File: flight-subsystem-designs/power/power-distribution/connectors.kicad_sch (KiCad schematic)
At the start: 36 parts, among them J1 Conn_02x07_Top_Bottom, J10 Conn_01x04, J2 Conn_02x26_Odd_Even, J3 Conn_01x02, J4 Conn_01x02, J5 Conn_01x02, J6 Conn_01x02, J7 Conn_02x26_Odd_Even, J8 Conn_01x04, J9 Conn_01x04, Q1 NMOS, Q2 NMOS

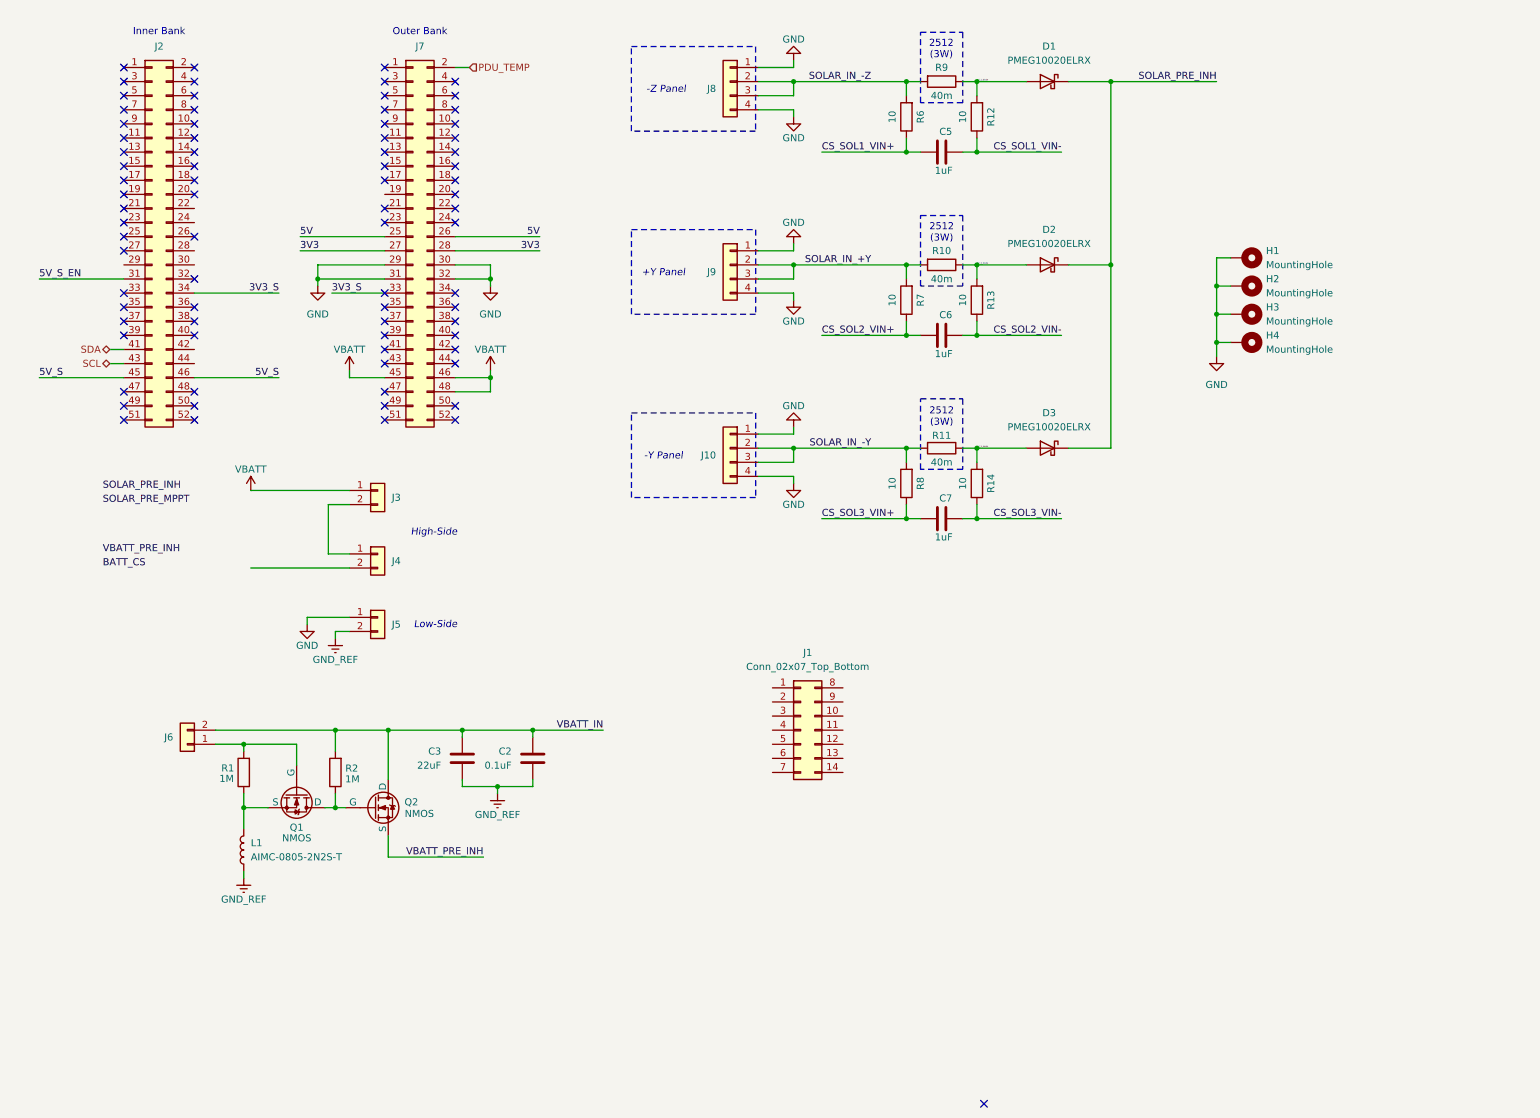
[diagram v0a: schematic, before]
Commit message: feat: PDU 4.0.0 (WIP)
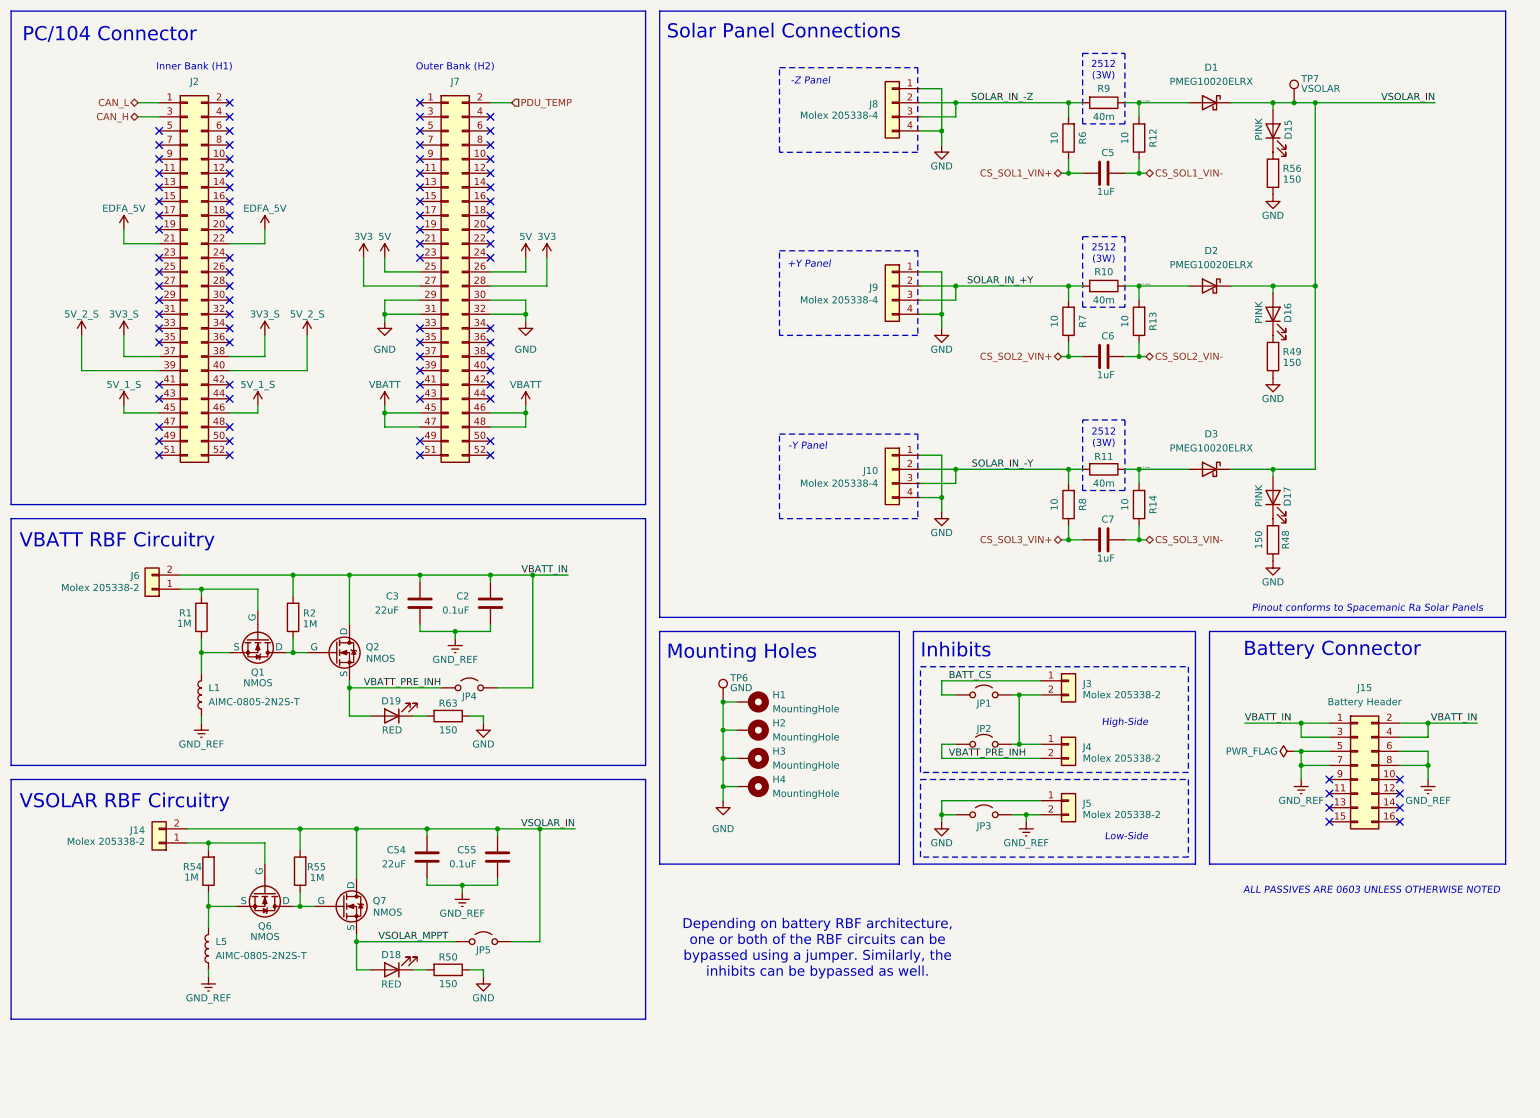
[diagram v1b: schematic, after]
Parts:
- removed J1: Conn_02x07_Top_Bottom, Connector_Harwin:Harwin_LTek-Male_2x07_P2.00mm_Vertical_StrainRelief, symbol Connector_Generic:Conn_02x07_Top_Bottom
- added C54: 22uF, Capacitor_SMD:C_0805_2012Metric, symbol Device:C
- added C55: 0.1uF, Capacitor_SMD:C_0805_2012Metric, symbol Device:C
- added D15, D16, D17: PINK, LED_SMD:LED_0603_1608Metric, symbol Device:LED
- added D18, D19: RED, LED_SMD:LED_0603_1608Metric, symbol Device:LED
- added J14: Molex 205338-2, Connector_Molex:Molex_Pico-Lock_205338-0002_1x02-1MP_P2.00mm_Horizontal, symbol Connector_Generic:Conn_01x02
- added J15: Battery Header, Connector_PinHeader_2.54mm:PinHeader_2x08_P2.54mm_Vertical, symbol Connector_Generic:Conn_02x08_Odd_Even
- added JP1, JP2, JP3, JP4, JP5: Jumper_2_Open, Jumper:SolderJumper-2_P1.3mm_Open_TrianglePad1.0x1.5mm, symbol Jumper:Jumper_2_Open
- added L5: AIMC-0805-2N2S-T, Inductor_SMD:L_0805_2012Metric, symbol Device:L
- added Q6, Q7: NMOS, Package_TO_SOT_SMD:TSOT-23, symbol Simulation_SPICE:NMOS
- added R48, R49, R50, R56, R63: 150, Resistor_SMD:R_0603_1608Metric, symbol Device:R
- added R54, R55: 1M, Resistor_SMD:R_0603_1608Metric, symbol Device:R
- added TP6: GND, TestPoint:TestPoint_Keystone_5000-5004_Miniature, symbol Connector:TestPoint
- added TP7: VSOLAR, TestPoint:TestPoint_Keystone_5000-5004_Miniature, symbol Connector:TestPoint
- J10, J8, J9: value Conn_01x04 -> Molex 205338-4
- J3, J4, J5: value Conn_01x02 -> Molex 205338-2
- J6: value Conn_01x02 -> Molex 205338-2; footprint (none) -> Connector_Molex:Molex_Pico-Lock_205338-0002_1x02-1MP_P2.00mm_Horizontal
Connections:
- net 3V3_S: now also J2.37 (Pin_37), J2.38 (Pin_38); no longer J2.34 (Pin_34), J7.33 (Pin_33)
- net BATT_CS: now also J3.1 (Pin_1), JP1.1 (A)
- net GND: now also JP3.1 (A), R48.1, R49.1, R50.1, R56.1, R63.1, TP6.1
- net GND_REF: now also C54.1, C55.1, J15.5 (Pin_5), J15.6 (Pin_6), J15.7 (Pin_7), J15.8 (Pin_8), JP3.2 (B), L5.1
- net VBATT: now also J7.47 (Pin_47); no longer J3.1 (Pin_1)
- net VBATT_IN: now also J15.1 (Pin_1), J15.2 (Pin_2), J15.3 (Pin_3), J15.4 (Pin_4), JP4.2 (B)
- net VBATT_PRE_INH: now also J4.2 (Pin_2), D19.2 (A), JP2.1 (A), JP4.1 (A)
- net at J3.2 (Pin_2), J4.1 (Pin_1): now also JP1.2 (B), JP2.2 (B)
- net CAN_L: now reaches J2.1 (Pin_1)
- net EDFA_5V: now reaches J2.21 (Pin_21)
- net EDFA_5V: now also J2.22 (Pin_22)
- net CAN_H: now reaches J2.3 (Pin_3)
- net 5V_2_S: now reaches J2.39 (Pin_39)
- net 5V_2_S: now also J2.40 (Pin_40)
- net 5V_S renamed 5V_1_S
- net 5V_S_EN: no longer names the net of J2.31 (Pin_31)
- net SCL: no longer names the net of J2.43 (Pin_43)
- net SDA: no longer names the net of J2.41 (Pin_41)
- net SOLAR_PRE_INH renamed VSOLAR_IN
- net VSOLAR_IN: now also C54.2, C55.2, D15.2 (A), D16.2 (A), D17.2 (A), J14.2 (Pin_2), JP5.2 (B), Q7.1 (D), R55.2, TP7.1
- new net: Q6.1 (D), Q7.2 (G), R55.1
- new net: D18.1 (K), R50.2
- new net: D16.1 (K), R49.2
- new net: J14.1 (Pin_1), Q6.2 (G), R54.2
- new net: D19.1 (K), R63.2
- new net: D17.1 (K), R48.2
- new net: L5.2, Q6.3 (S), R54.1
- new net: D15.1 (K), R56.2
- new net VSOLAR_MPPT: D18.2 (A), JP5.1 (A), Q7.3 (S)
- no-connect marks 79 -> 89
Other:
- note added: "ALL PASSIVES ARE 0603 UNLESS OTHERWISE NOTED"
- note added: "Battery Connector"
- note added: "Depending on battery RBF architecture, one or both of the RBF circuits can be bypassed using a jumper. Similarly, the inhibits can be bypassed as well."
- note added: "Inhibits"
- note added: "Inner Bank (H1)"
- note added: "Mounting Holes"
- note added: "Outer Bank (H2)"
- note added: "PC/104 Connector"
- note added: "Pinout conforms to Spacemanic Ra Solar Panels"
- note added: "Solar Panel Connections"
- note added: "VBATT RBF Circuitry"
- note added: "VSOLAR RBF Circuitry"
- note removed: "Inner Bank"
- note removed: "Outer Bank"
- moved on the sheet: C2, C3, C5, C6, C7, D1, D2, D3, H1, H2, H3, H4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

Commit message: shi
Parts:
- removed C2, C55: 0.1uF, Capacitor_SMD:C_0805_2012Metric, symbol Device:C
- removed C3, C54: 22uF, Capacitor_SMD:C_0805_2012Metric, symbol Device:C
- removed D18, D19: RED, LED_SMD:LED_0603_1608Metric, symbol Device:LED
- removed J14, J3, J4, J5, J6: Molex 205338-2, Connector_Molex:Molex_Pico-Lock_205338-0002_1x02-1MP_P2.00mm_Horizontal, symbol Connector_Generic:Conn_01x02
- removed JP1, JP2, JP3, JP4, JP5: Jumper_2_Open, Jumper:SolderJumper-2_P1.3mm_Open_TrianglePad1.0x1.5mm, symbol Jumper:Jumper_2_Open
- removed L1, L5: AIMC-0805-2N2S-T, Inductor_SMD:L_0805_2012Metric, symbol Device:L
- removed Q1, Q2, Q6, Q7: NMOS, Package_TO_SOT_SMD:TSOT-23, symbol Simulation_SPICE:NMOS
- removed R1, R2, R54, R55: 1M, Resistor_SMD:R_0603_1608Metric, symbol Device:R
- removed R50, R63: 150, Resistor_SMD:R_0603_1608Metric, symbol Device:R
- added J13, J19: RBF, Connector_Molex:Molex_PicoBlade_53047-0210_1x02_P1.25mm_Vertical, symbol Connector_Generic:Conn_01x02
- added J16, J17: NO, Connector_Molex:Molex_PicoBlade_53047-0210_1x02_P1.25mm_Vertical, symbol Connector_Generic:Conn_01x02
- added J18: NC, Connector_Molex:Molex_PicoBlade_53047-0210_1x02_P1.25mm_Vertical, symbol Connector_Generic:Conn_01x02
- added Q8: PMOS, Package_SO:TSOP-6_1.65x3.05mm_P0.95mm, symbol Simulation_SPICE:PMOS
- added Q9: NMOS, Package_SO:TSOP-6_1.65x3.05mm_P0.95mm, symbol Simulation_SPICE:NMOS
- added R64, R65, R66: 100k, Resistor_SMD:R_0603_1608Metric, symbol Device:R
- added U22: SI3407DV, Package_SO:TSOP-6_1.65x3.05mm_P0.95mm, symbol pdu:SI3407DV-T1-GE3
- J10, J8, J9: footprint Connector_Molex:Molex_Pico-Lock_205338-0004_1x04-1MP_P2.00mm_Horizontal -> Connector_Molex:Molex_PicoBlade_53047-0410_1x04_P1.25mm_Vertical
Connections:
- net BATT_CS: now also Q8.1 (D), Q8.2 (D), Q8.5 (D), Q8.6 (D)
- net GND: now also J13.1 (Pin_1), J16.1 (Pin_1), J17.1 (Pin_1), J19.1 (Pin_1), Q9.3 (S), R65.1
- net GND_REF: now also Q9.1 (D)
- net VBATT: now also J18.2 (Pin_2)
- net VBATT_IN: now also Q8.4 (S), R64.1
- net VSOLAR_IN: now also R66.1, U22.4 (S1); no longer D15.2 (A), D16.2 (A), D17.2 (A)
- net VSOLAR_MPPT: now also U22.1 (D2), U22.2 (D3), U22.5 (D4), U22.6 (D1)
- net sol_1_diode: now also D15.2 (A)
- net sol_2_diode: now also D16.2 (A)
- net sol_3_diode: now also D17.2 (A)
- new net: J19.2 (Pin_2), R66.2, U22.3 (G)
- new net: J13.2 (Pin_2), J16.2 (Pin_2), J17.2 (Pin_2), Q8.3 (G), R64.2
- new net: J18.1 (Pin_1), Q9.2 (G), R65.2
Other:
- note removed: "High-Side"
- note removed: "Inhibits"
- note removed: "Low-Side"
- note removed: "VSOLAR RBF Circuitry"
- moved on the sheet: D1, D15, D16, D17, D2, D3, J15, R48, R49, R56, TP7
